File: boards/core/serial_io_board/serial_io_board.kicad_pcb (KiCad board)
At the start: 2 copper layers, 95.2 x 95.2 mm, 37 parts, among them J1 Exp. Conn. A, J2 Exp. Conn. B, J3 Power, J4 ~{RTS}/~{DTR} SELECT, J5 FTDI VCC SELECT, J6 FTDI, J7 COM1, SW1 I/O Address / IRQ selection, SW2 FTDI_PT, U1 74LS04, U2 74LS139, U3 74LS688, U4 16550, U5 MAX232, X1 7.3728MHz

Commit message: * Working on new powerdistribution method.
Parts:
- removed CP3: 10uF, Capacitor_THT:CP_Radial_D5.0mm_P2.50mm
- removed CP4: 0.1uF, Capacitor_THT:CP_Radial_D5.0mm_P2.50mm
- removed J5: FTDI VCC SELECT, Connector_PinHeader_2.54mm:PinHeader_1x03_P2.54mm_Vertical
- J3: footprint Connector_IDC:IDC-Header_2x10_P2.54mm_Horizontal -> footprints:TE_171826-4
- R1: value 470 -> 1k
- moved J3 89.5 mm to (120.1, 105.2), turned to 90 degrees
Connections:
- J3 pad 1: /+3.3V -> unconnected-(J3-Pin_1-Pad1)
- J3 pad 2: /+3.3V2 -> /GND
- SW2 pad 3: /SUPVCC -> /+5V
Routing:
- net /SUPVCC: track 47.5 -> 0.00 mm
- net /+5V: track 322.4 -> 353.6 mm
- net /+3.3V: track 29.3 -> 0.00 mm
- net /GND: track 183.5 -> 171.7 mm
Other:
- board text added: "+5V"
- board text added: "GND"
- board text added: "NC"

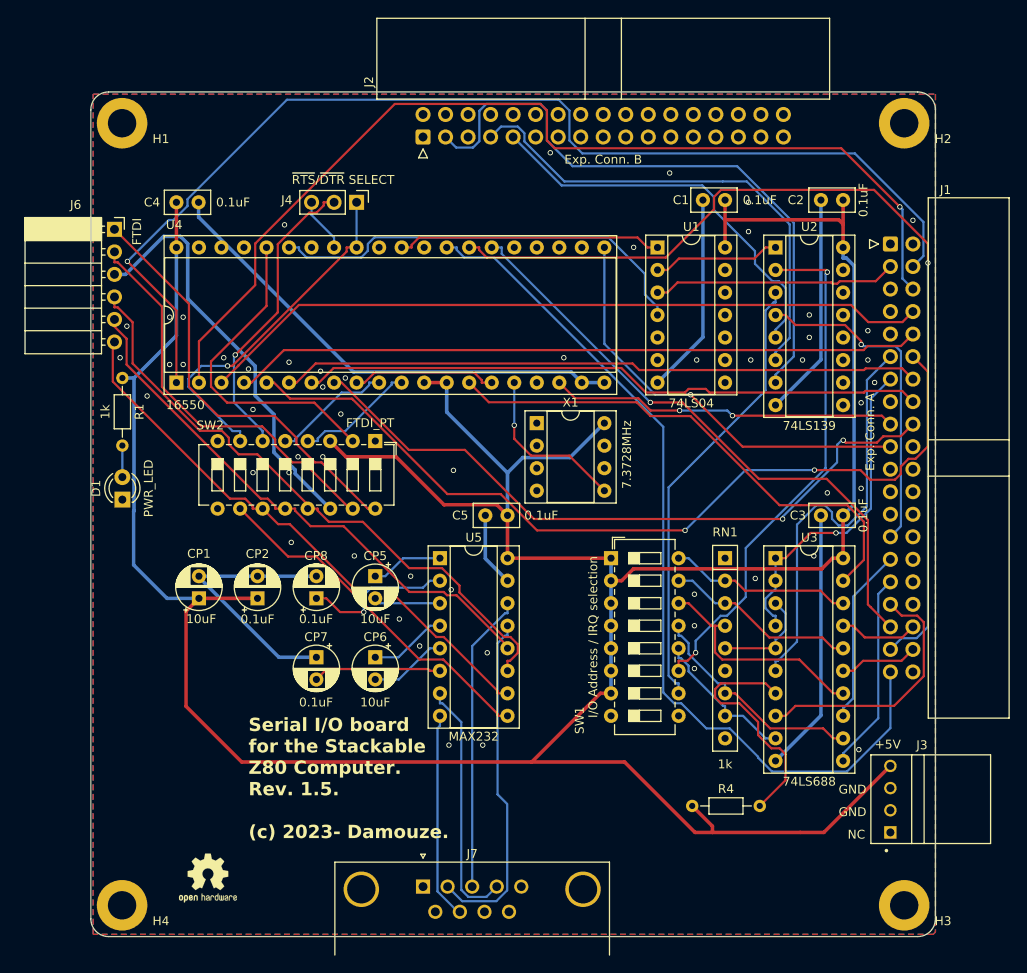
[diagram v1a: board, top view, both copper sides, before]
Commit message: Added expansion connector C and designed some new boards around it.
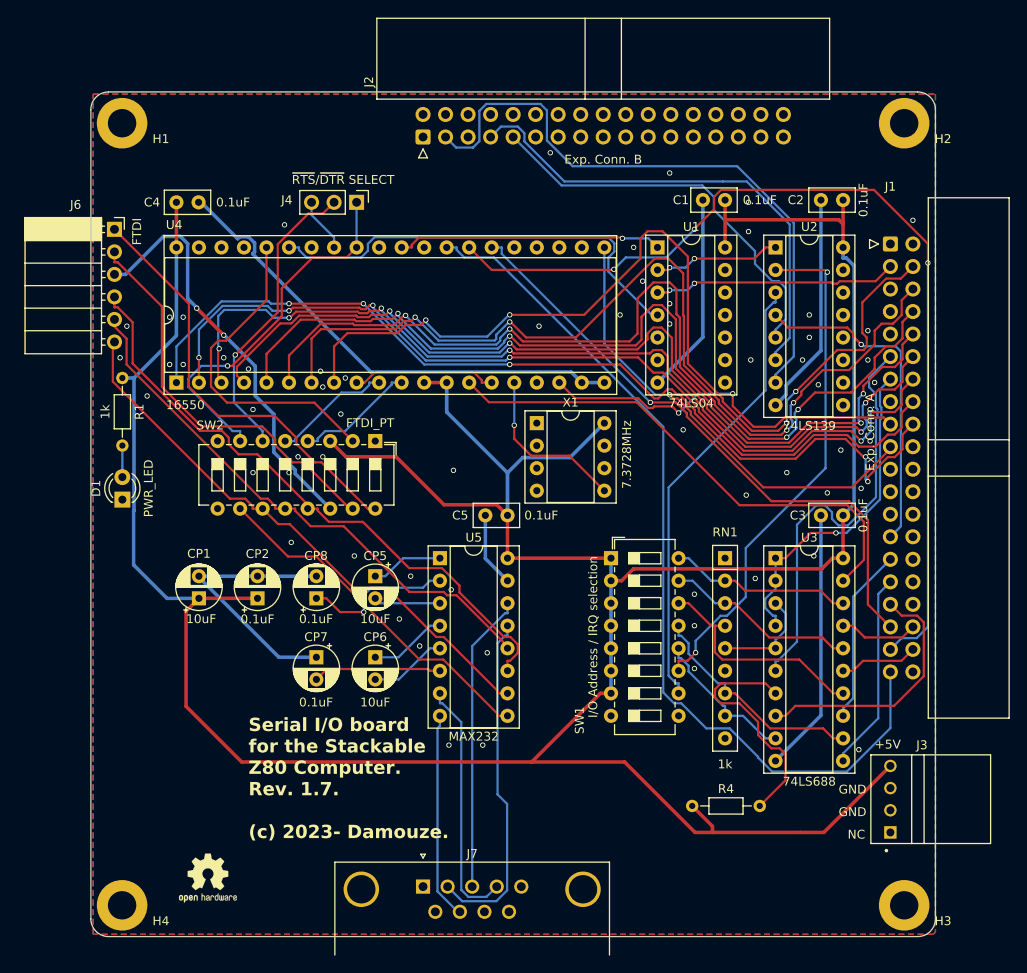
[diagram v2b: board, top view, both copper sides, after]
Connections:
- net Net-(J4-Pin_2) renamed /~{FTDI_DTR}
- U4 pad 1: /B_D7 -> /B_D0
- U4 pad 2: /B_D6 -> /B_D1
- U4 pad 3: /B_D5 -> /B_D2
- U4 pad 4: /B_D4 -> /B_D3
- U4 pad 5: /B_D3 -> /B_D4
- U4 pad 6: /B_D2 -> /B_D5
- U4 pad 7: /B_D1 -> /B_D6
- U4 pad 8: /B_D0 -> /B_D7
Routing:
- net /B_D2: track 72.1 -> 103.3 mm, vias 0 -> 6
- net /B_D1: track 70.6 -> 100.4 mm, vias 0 -> 4
- net /B_D0: track 77.6 -> 106.0 mm, vias 2 -> 5
- net /B_D4: track 77.7 -> 102.9 mm, vias 0 -> 4
- net /B_D5: track 82.9 -> 104.8 mm, vias 0 -> 4
- net /B_D7: track 126.9 -> 107.4 mm, vias 1 -> 4
- net /B_D6: track 114.2 -> 105.4 mm, vias 1 -> 4
- net /~{B_RD}: track 47.9 -> 52.1 mm
- net /~{B_WR}: track 39.3 -> 42.9 mm
- net /B_D3: track 97.6 -> 100.9 mm, vias 2 -> 4
- net /~{UART_RTS}: track 40.4 -> 42.0 mm
- net /B_A1: track 107.4 -> 108.4 mm, vias 1 -> 3
- net /UART_RESET: track 49.2 -> 50.0 mm
- net /~{B_M1}: track 46.7 -> 47.5 mm
- net /~{UART_CTS}: track 36.8 -> 37.3 mm
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
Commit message: Updated serial I/O board last weekend.
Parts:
- SW1: value I/O Address / IRQ selection -> I/O Address / IRQ select
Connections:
- SW1 pad 10: /IRQ0_S -> /IRQ1_S
- SW1 pad 11: /IRQ1_S -> /IRQ0_S
- SW1 pad 12: /R_A3 -> /R_A7
- SW1 pad 13: /R_A4 -> /R_A6
- SW1 pad 15: /R_A6 -> /R_A4
- SW1 pad 16: /R_A7 -> /R_A3
- U2 pad 13: unconnected-(U2B-A1-Pad13) -> /GND
- U2 pad 14: unconnected-(U2B-A0-Pad14) -> /GND
- U2 pad 15: unconnected-(U2B-E-Pad15) -> /+5V
- U2 pad 2: /IRQ1_S -> /IRQ0_S
- U2 pad 3: /IRQ0_S -> /IRQ1_S
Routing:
- net /GND: track 171.9 -> 0.00 mm, vias 61 -> 29
- net /~{R_M1}: track 27.0 -> 14.8 mm, vias 0 -> 1
- net /R_A3: track 16.8 -> 26.7 mm, vias 0 -> 1
- net /R_A7: track 20.7 -> 30.2 mm
- net /IRQ0_S: track 51.0 -> 58.9 mm, vias 0 -> 2
- net /IRQ1_S: track 58.7 -> 50.9 mm, vias 2 -> 0
- net /R_A4: track 25.8 -> 32.0 mm, vias 0 -> 2
- net /B_D7: track 107.4 -> 111.7 mm
- net /B_D5: track 104.8 -> 107.4 mm
- net /+5V: track 353.6 -> 356.0 mm
- net /B_D6: track 105.4 -> 107.1 mm
- net /~{DTR}: track 63.9 -> 62.3 mm
- net /B_D4: track 102.9 -> 104.5 mm
- net /B_D1: track 100.4 -> 101.9 mm
- net /B_D0: track 106.0 -> 107.5 mm
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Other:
- rule pad_to_mask_clearance: 0.2 -> 0
- board text removed: "SW 1.1-1.5: I/O BASE ADDRESS SELECTION Base address in increments of 8, selectable from 0x00 through 0xF8. Firmware default is 0x80. SW 1.6/1.7: IRQ SELECTION SW1.6 SW1.7 0 0 ~{INT} 0 1 ~{INT4} 1 0 ~{INT5} 1 1 ~{INT7}"
